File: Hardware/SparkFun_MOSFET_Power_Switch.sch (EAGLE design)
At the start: 40 parts, among them J1 PTH, J3 5.5x2.1mm Barrel, J4 SMD, Q1 600mA/40V, Q2 100A/100V/6.8mΩ, U1 LMR14203

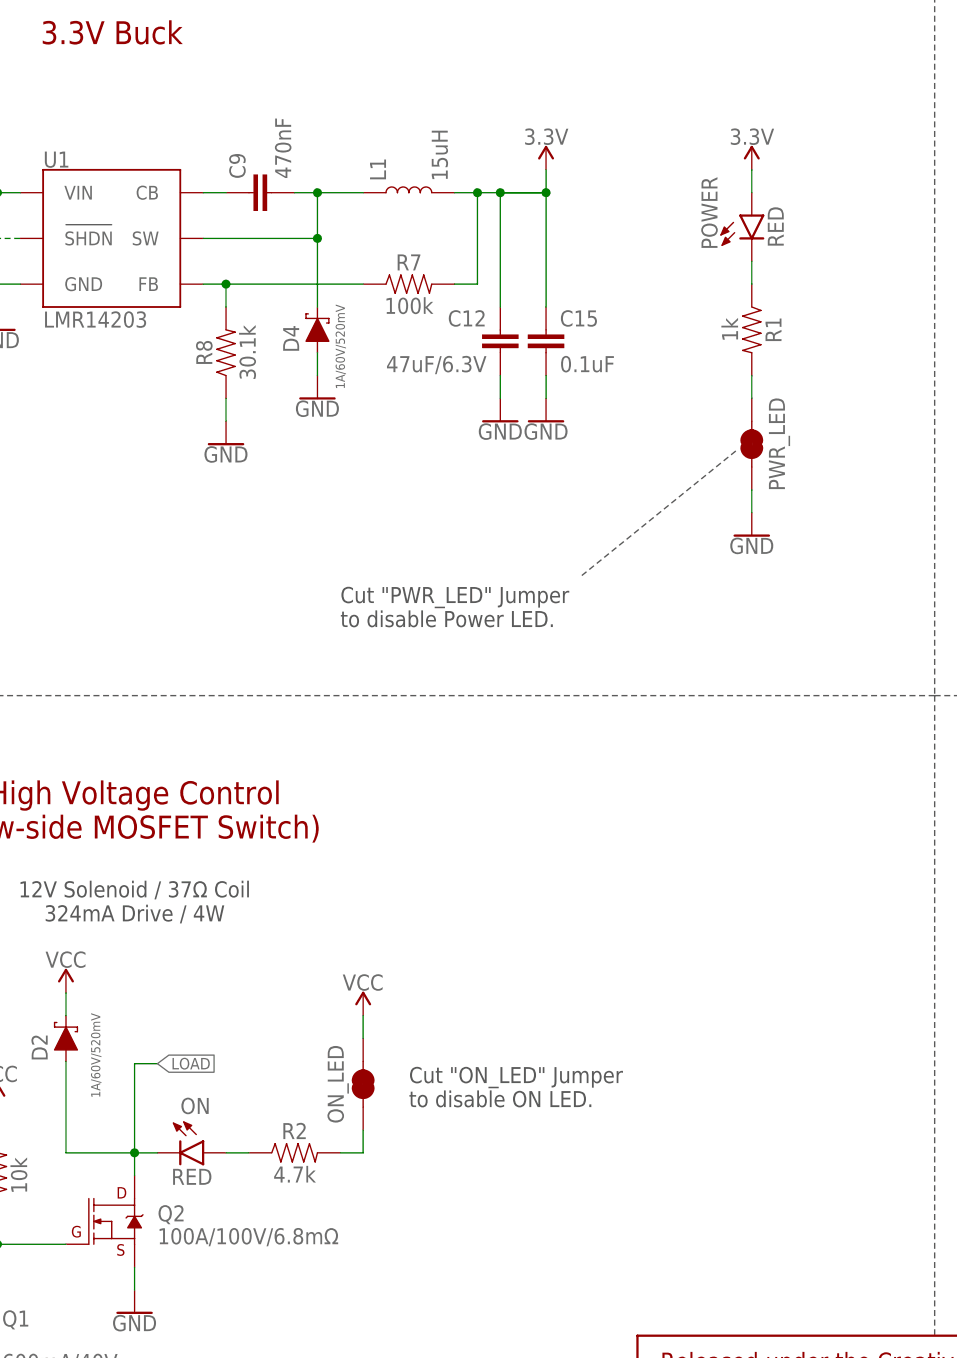
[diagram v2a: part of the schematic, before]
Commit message: updated to new KB red resistor
-updated red led and limiting resistor
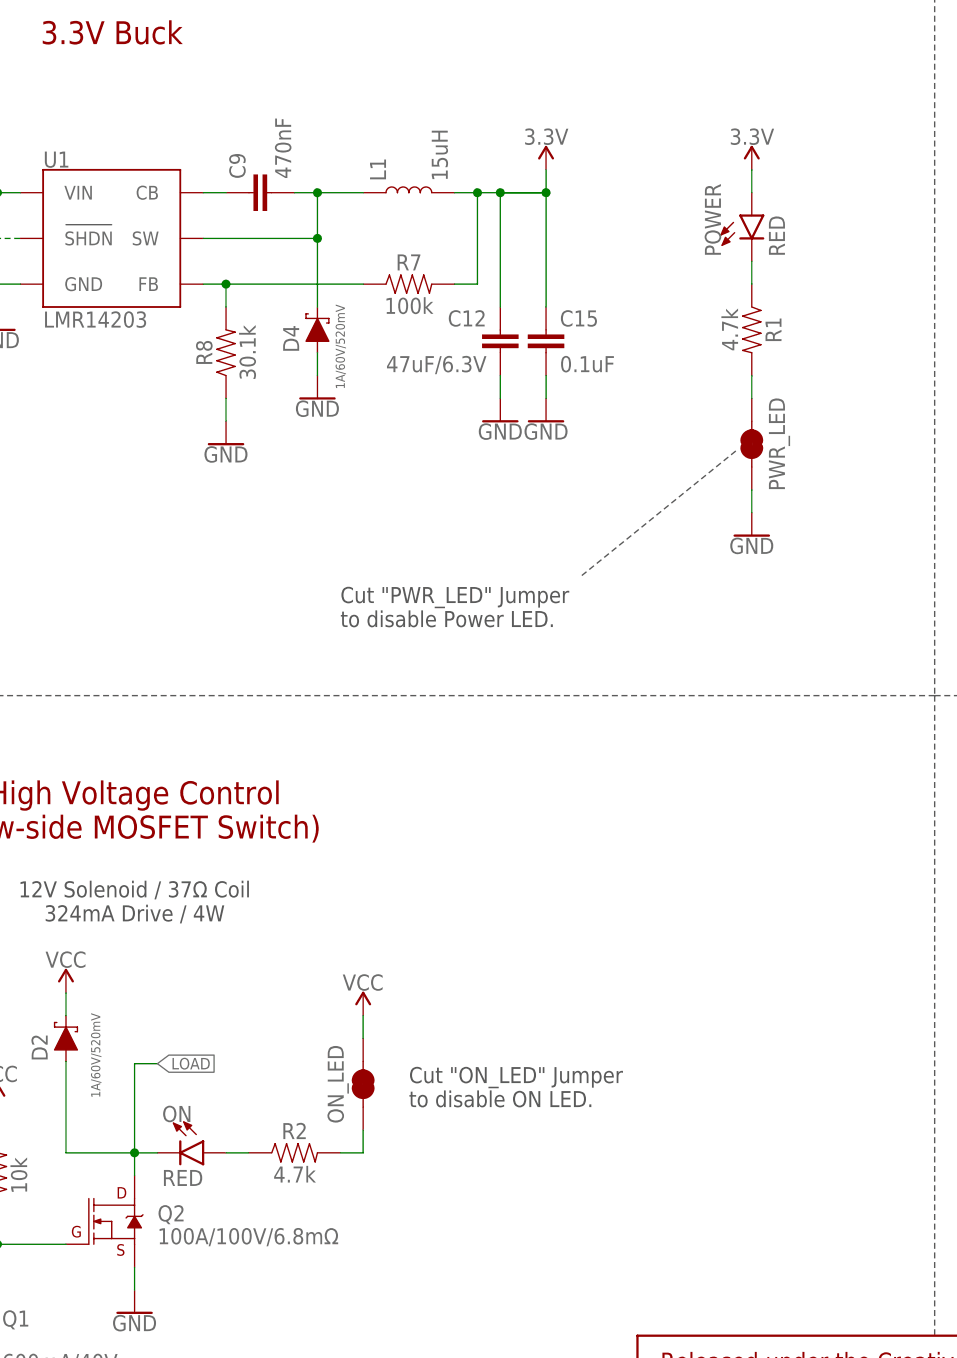
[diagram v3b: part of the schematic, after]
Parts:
- ON, POWER: device SparkFun-LED:LED-RED0603 -> SparkFun-LED:LED-RED_0603-KB
- R1: value 1k -> 4.7k; device SparkFun-Resistors:1KOHM-0603-1/10W-1% -> SparkFun-Resistors:4.7KOHM-0603-1/10W-1%
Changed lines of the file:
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@@
 <part name="H4" library="SparkFun-Hardware" deviceset="STAND-OFF" device=""/>
 <part name="H3" library="SparkFun-Hardware" deviceset="STAND-OFF" device=""/>
-<part name="ON" library="SparkFun-LED" deviceset="LED-RED" device="0603" value="RED"/>
+<part name="ON" library="SparkFun-LED" deviceset="LED-RED" device="_0603-KB" value="RED"/>
 <part name="R2" library="SparkFun-Resistors" deviceset="4.7KOHM" device="-0603-1/10W-1%" value="4.7k"/>
 <part name="R7" library="SparkFun-Resistors" deviceset="100KOHM" device="-0603-1/10W-1%" value="100k"/>
@@
 <part name="MEAS" library="SparkFun-Jumpers" deviceset="JUMPER-COMBO_2_NC_TRACE" device=""/>
 <part name="SUPPLY8" library="SparkFun-PowerSymbols" deviceset="3.3V" device=""/>
-<part name="POWER" library="SparkFun-LED" deviceset="LED-RED" device="0603" value="RED"/>
-<part name="R1" library="SparkFun-Resistors" deviceset="1KOHM" device="-0603-1/10W-1%" value="1k"/>
+<part name="POWER" library="SparkFun-LED" deviceset="LED-RED" device="_0603-KB" value="RED"/>
+<part name="R1" library="SparkFun-Resistors" deviceset="4.7KOHM" device="-0603-1/10W-1%" value="4.7k"/>
 <part name="GND2" library="SparkFun-PowerSymbols" deviceset="GND" device=""/>
 <part name="J4" library="SparkFun-Connectors" deviceset="CONN_04" device="SMD_STRAIGHT_COMBO" value="SMD"/>
@@
 <instance part="H3" gate="G$1" x="243.84" y="27.94" smashed="yes"/>
 <instance part="ON" gate="G$1" x="99.06" y="55.88" smashed="yes" rot="R270">
-<attribute name="NAME" x="96.52" y="60.198" size="1.778" layer="95" font="vector"/>
-<attribute name="VALUE" x="95.504" y="54.102" size="1.778" layer="96" font="vector" align="top-left"/>
+<attribute name="NAME" x="94.488" y="59.309" size="1.778" layer="95" font="vector"/>
+<attribute name="VALUE" x="94.488" y="53.975" size="1.778" layer="96" font="vector" align="top-left"/>
 </instance>
 <instance part="R2" gate="G$1" x="109.22" y="55.88" smashed="yes">
@@
 </instance>
 <instance part="POWER" gate="G$1" x="160.02" y="160.02" smashed="yes">
-<attribute name="NAME" x="156.21" y="156.21" size="1.778" layer="95" font="vector" rot="R90"/>
-<attribute name="VALUE" x="161.798" y="156.464" size="1.778" layer="96" font="vector" rot="R90" align="top-left"/>
+<attribute name="NAME" x="156.591" y="155.448" size="1.778" layer="95" font="vector" rot="R90"/>
+<attribute name="VALUE" x="161.925" y="155.448" size="1.778" layer="96" font="vector" rot="R90" align="top-left"/>
 </instance>
 <instance part="R1" gate="G$1" x="160.02" y="147.32" smashed="yes" rot="R270">

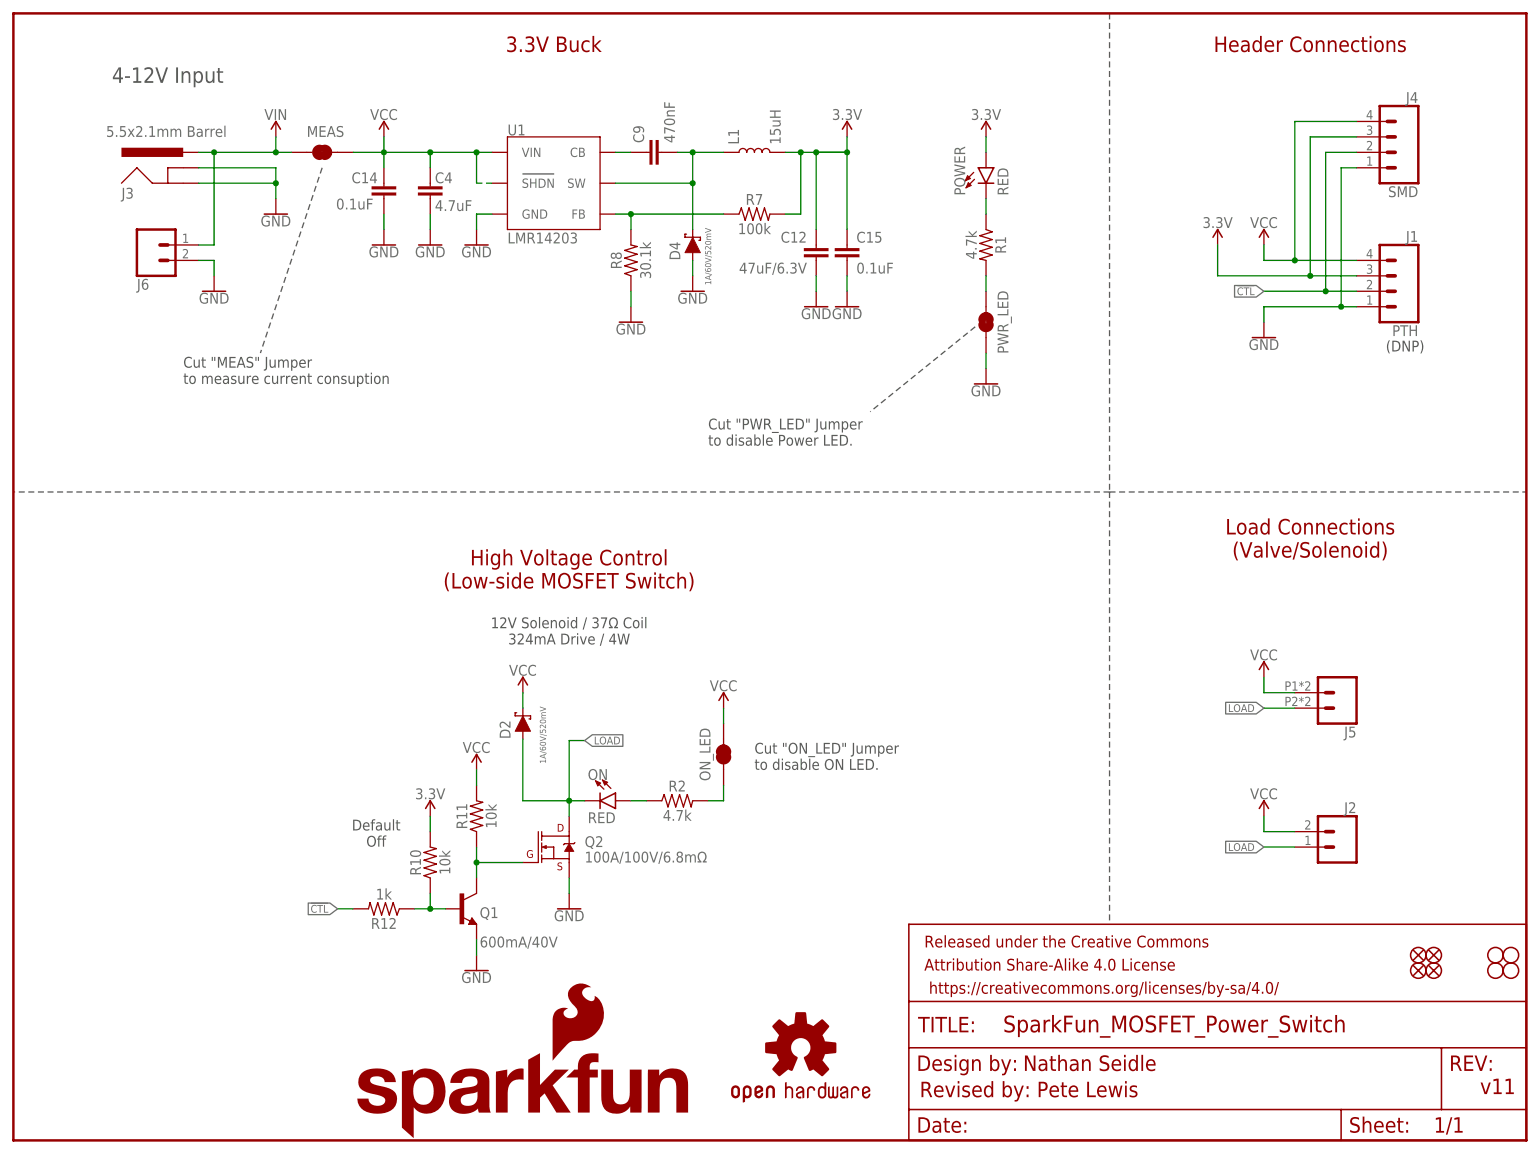
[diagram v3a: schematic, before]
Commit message: Group Review mods round one
-Powered ON LED from 3.3V and controlled via CTL net.
-Moved GND/VIN PTH headers away from under the barrel jack for easier access
-routed some of load path with polygons to avoid sharp 90 degree turns in traces
-moved MEAS jumper to allow direct GND pour path from MOSFET to Barrel jack GND pads
-added "+" and "-" silk to MEAS jumper PTH header
-enlarged board to 1.5" square shape
-spaced out components near BJT for better DFM
-nudged some vias to avoid silk
-corrected voltage input range to "4.5-12V".
-added ordering instructions
-Larger logos
-added and updated measures
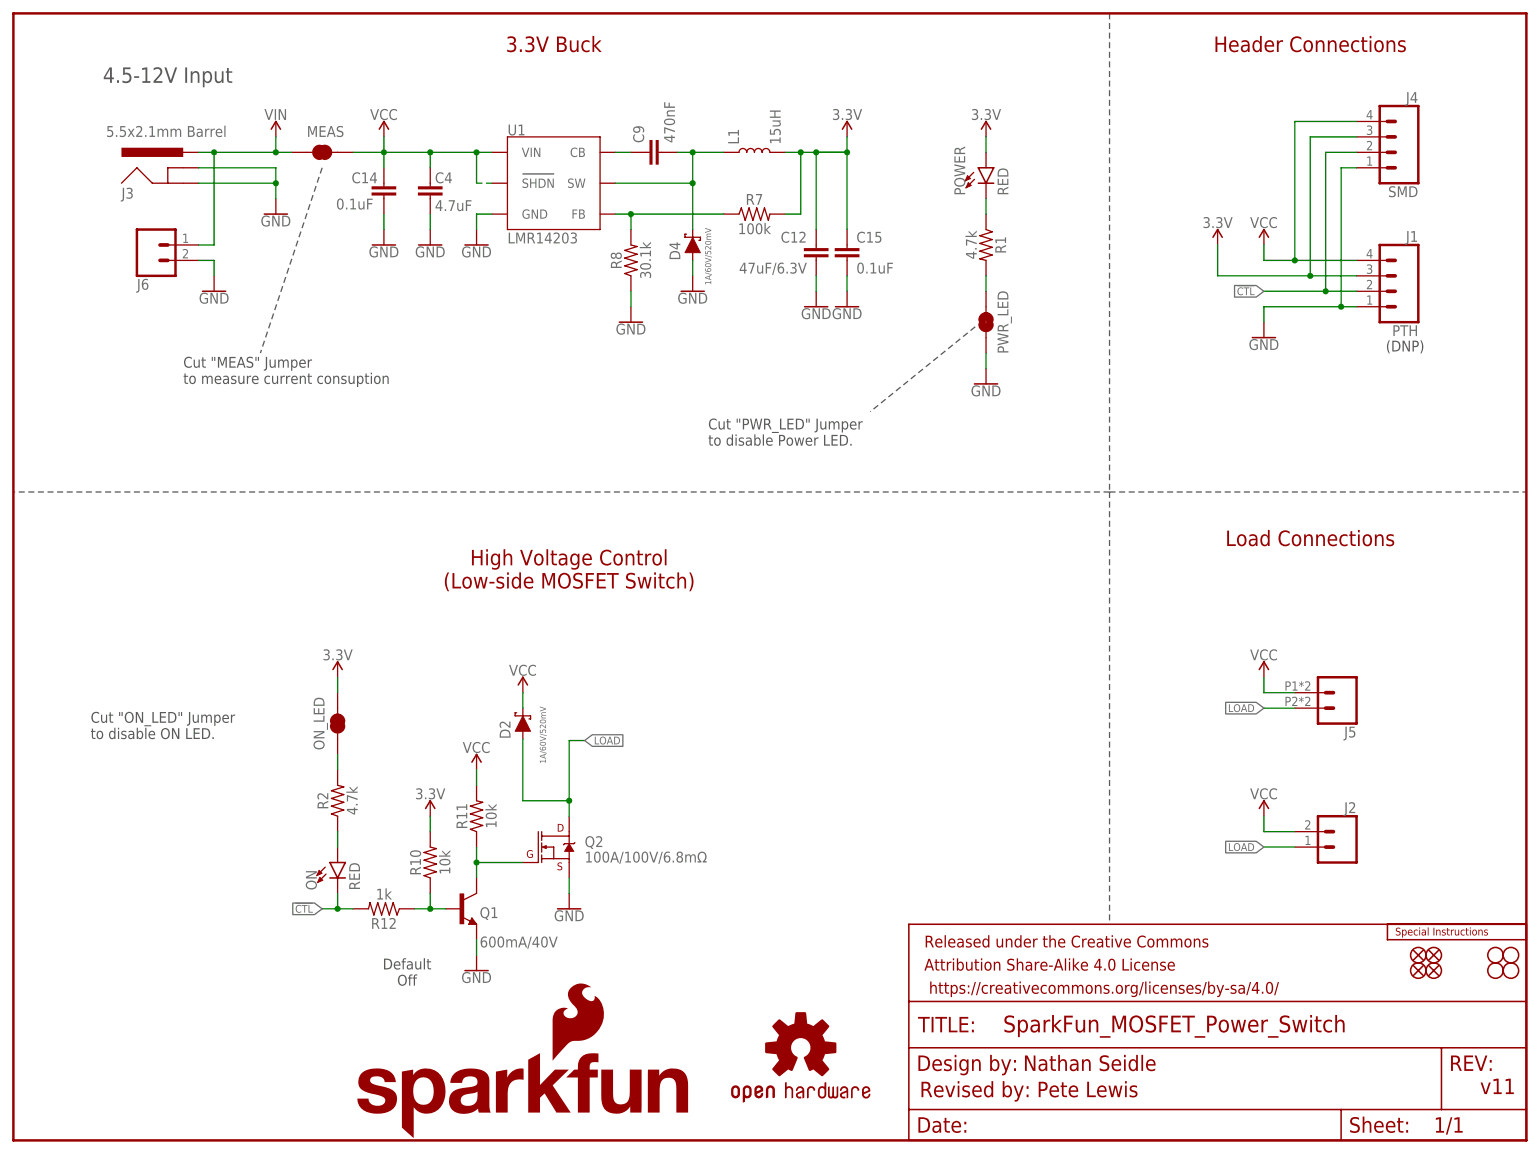
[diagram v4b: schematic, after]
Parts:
- added LOGO3: SPECIAL_INSTRUCTIONS-ORDERING, SparkFun-Aesthetics:SPECIAL_INSTRUCTIONS-ORDERING
- LOGO1: value OSHW-LOGOS -> OSHW-LOGOM; device SparkFun-Aesthetics:OSHW-LOGOS -> SparkFun-Aesthetics:OSHW-LOGOM
- LOGO2: value SFE_LOGO_NAME_FLAME.1_INCH -> SFE_LOGO_NAME_FLAME.2_INCH; device SparkFun-Aesthetics:SFE_LOGO_NAME_FLAME.1_INCH -> SparkFun-Aesthetics:SFE_LOGO_NAME_FLAME.2_INCH
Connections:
- net !CTL: now also ON.C
- net 3.3V: now also ON_LED.2
- net LOAD: no longer ON.C
- net VCC: no longer ON_LED.2
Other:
- note added: "4.5-12V Input"
- note added: "Load Connections"
- note removed: "12V Solenoid / 37Ω Coil 324mA Drive / 4W"
- note removed: "4-12V Input"
- note removed: "Load Connections (Valve/Solenoid)"
- moved on the sheet: ON, ON_LED, R2
